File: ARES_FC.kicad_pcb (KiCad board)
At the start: 2 copper layers, 57.2 x 57.2 mm, 67 parts, among them J1 SWD, J2 TYPE-C-31-M-12, J3 FC_M/P, J4 5V, J5 GND, J6 FC_RF, J7 Conn_01x04_Pin, J8 Conn_01x04_Pin, U1 STM32F401CCU6, U2 AMS1117-3.3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

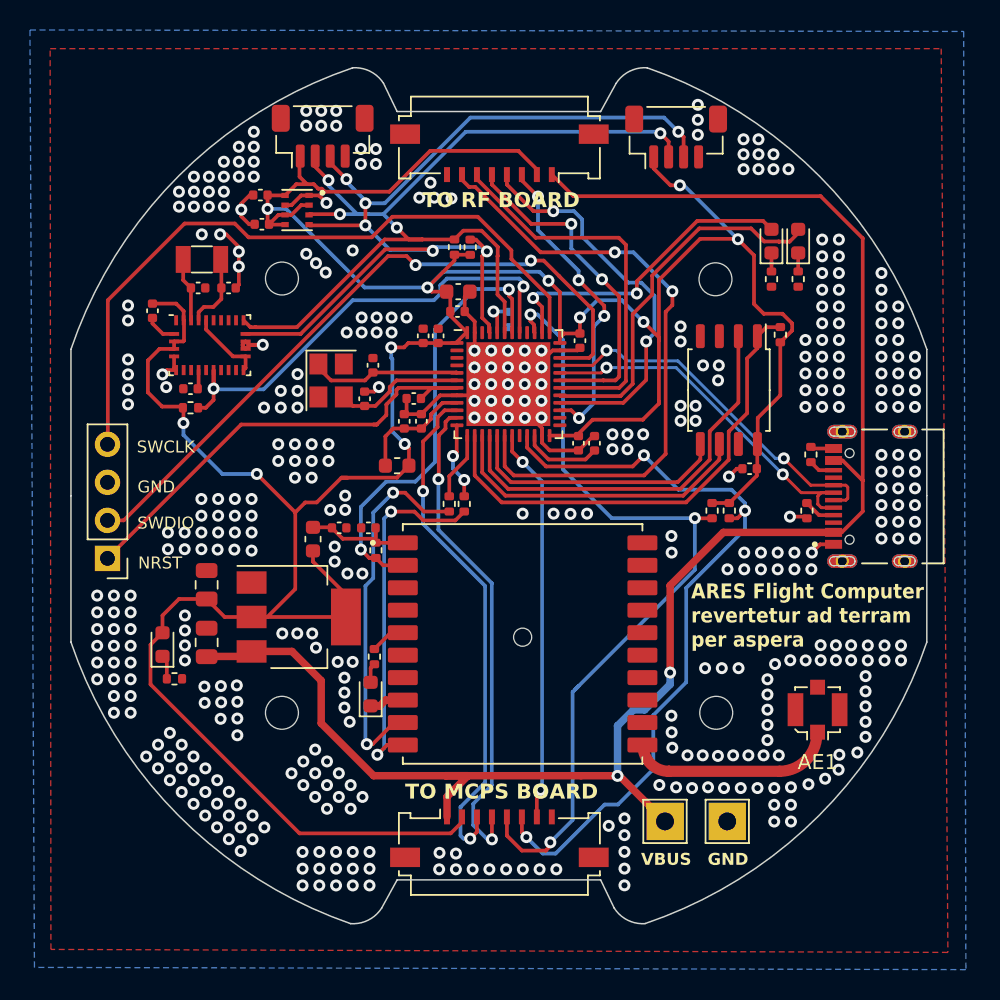
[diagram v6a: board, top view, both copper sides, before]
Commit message: TVS Diodes at connector lines
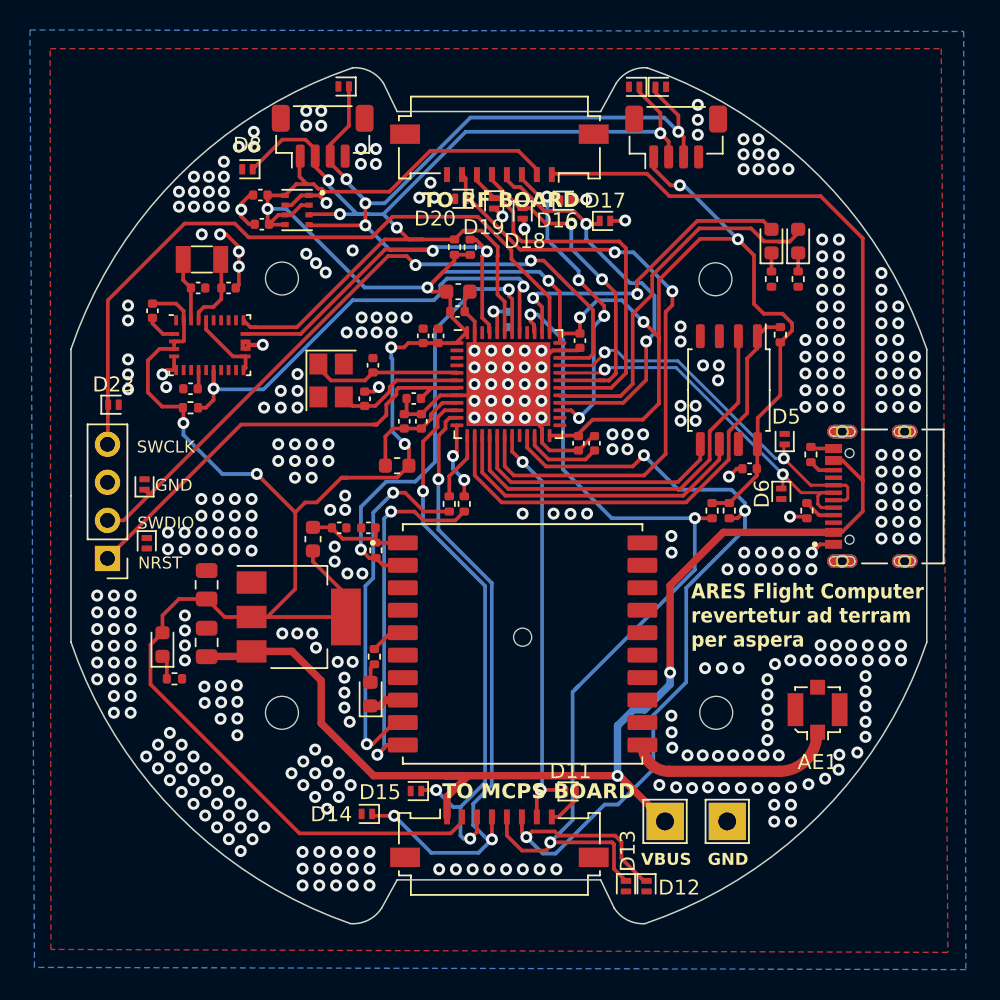
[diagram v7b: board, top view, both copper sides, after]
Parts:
- added D10: PESD3V3U1UL, Diode_SMD:D_SOD-882, F.Cu at (160.8, 72.2)
- added D11: PESD3V3U1UL, Diode_SMD:D_SOD-882, F.Cu at (154.8, 119.2)
- added D12: PESD3V3U1UL, Diode_SMD:D_SOD-882, F.Cu at (159.8, 125.6)
- added D13: PESD3V3U1UL, Diode_SMD:D_SOD-882, F.Cu at (158.4, 125.6)
- added D14: PESD3V3U1UL, Diode_SMD:D_SOD-882, F.Cu at (141.2, 120.8)
- added D15: PESD3V3U1UL, Diode_SMD:D_SOD-882, F.Cu at (144.4, 119.2)
- added D16: PESD3V3U1UL, Diode_SMD:D_SOD-882, F.Cu at (154.4, 79.8)
- added D17: PESD3V3U1UL, Diode_SMD:D_SOD-882, F.Cu at (157.1, 81.2)
- added D18: PESD3V3U1UL, Diode_SMD:D_SOD-882, F.Cu at (151.6, 80.7)
- added D19: PESD3V3U1UL, Diode_SMD:D_SOD-882, F.Cu at (149.7, 80.0)
- added D20: PESD3V3U1UL, Diode_SMD:D_SOD-882, F.Cu at (147.4, 79.7)
- added D21: PESD3V3U1UL, Diode_SMD:D_SOD-882, F.Cu at (126.5, 102.7)
- added D22: PESD3V3U1UL, Diode_SMD:D_SOD-882, F.Cu at (126.3, 98.8)
- added D23: PESD3V3U1UL, Diode_SMD:D_SOD-882, F.Cu at (124.2, 93.4)
- added D5: PESD3V3U1UL, Diode_SMD:D_SOD-882, F.Cu at (169.1, 95.7)
- added D6: PESD3V3U1UL, Diode_SMD:D_SOD-882, F.Cu at (168.8, 99.4)
- added D7: PESD3V3U1UL, Diode_SMD:D_SOD-882, F.Cu at (139.6, 72.2)
- added D8: PESD3V3U1UL, Diode_SMD:D_SOD-882, F.Cu at (133.2, 77.7)
- added D9: PESD3V3U1UL, Diode_SMD:D_SOD-882, F.Cu at (159.0, 72.2)
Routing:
- net /MOTOR_SCL: track 51.8 -> 62.0 mm
- net /S2_MP: track 33.1 -> 42.6 mm, vias 2 -> 3
- net /SDA: track 62.6 -> 72.0 mm
- net /SCL: track 65.8 -> 74.6 mm
- net /MOTOR_SDA: track 55.1 -> 62.1 mm
- net GND: track 61.0 -> 67.2 mm, vias 412 -> 398
- net /S1_MP: track 34.6 -> 37.7 mm, vias 2 -> 3
- net /MOTOR_NRST: track 26.4 -> 28.1 mm
- net /S1_RF: track 20.7 -> 22.0 mm
- net /USB_D-: track 24.7 -> 25.7 mm
- net /USB_D+: track 25.2 -> 26.2 mm
- net /S2_RF: track 26.5 -> 27.3 mm
- net /RX_RADIO: track 22.6 -> 22.0 mm
- net /RADIO_NRST: track 42.2 -> 42.8 mm

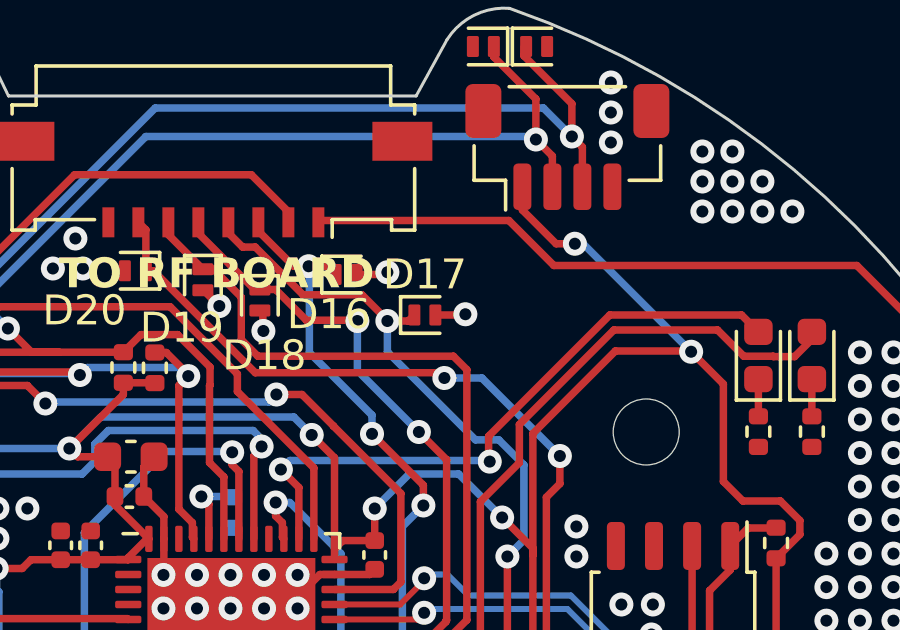
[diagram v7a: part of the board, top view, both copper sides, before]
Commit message: Update PCB design and project settings
Adjusted user text position and removed a segment in the PCB layout. Updated visible layers in the project layout file and added several DRC exclusions in the project settings. Lock files for PCB and schematic were added.
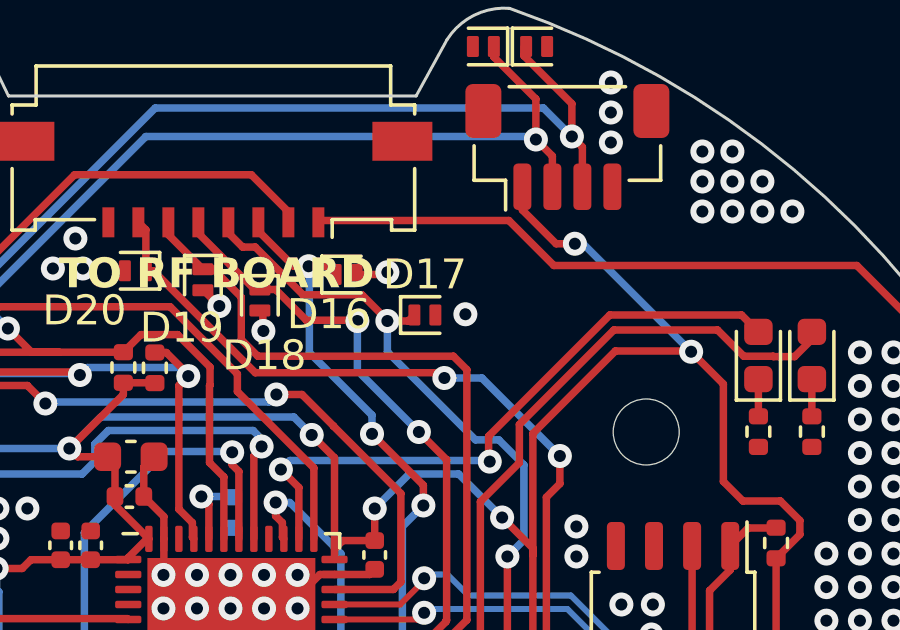
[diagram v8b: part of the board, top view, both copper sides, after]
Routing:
- net GND: track 67.2 -> 66.2 mm
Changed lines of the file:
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@@
 		)
 		(fp_text user "${REFERENCE}"
-			(at -0.127 -1.35 0)
+			(at -0.127 -1.2 0)
 			(layer "F.Fab")
 			(effects
@@
 		(width 0.25)
 		(layer "F.Cu")
-		(net 2)
-	)
-	(segment
-		(start 157.4 81.15)
-		(end 158.375 81.15)
-		(width 0.25)
-		(layer "F.Cu")
